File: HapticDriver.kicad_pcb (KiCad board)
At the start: 4 copper layers, 39 x 27 mm, 31 parts, among them J1 Conn_01x02_Socket, J14 USB_C_Receptacle_USB2.0, J3 BATT PWR, SW1 BOOT, SW2 EN, U1 ESP32-S3-WROOM-2, U12 DRV8912QPWPRQ1, U2 TPS561201DDCR, U3 DRV8912QPWPRQ1, U4 MAX98357A

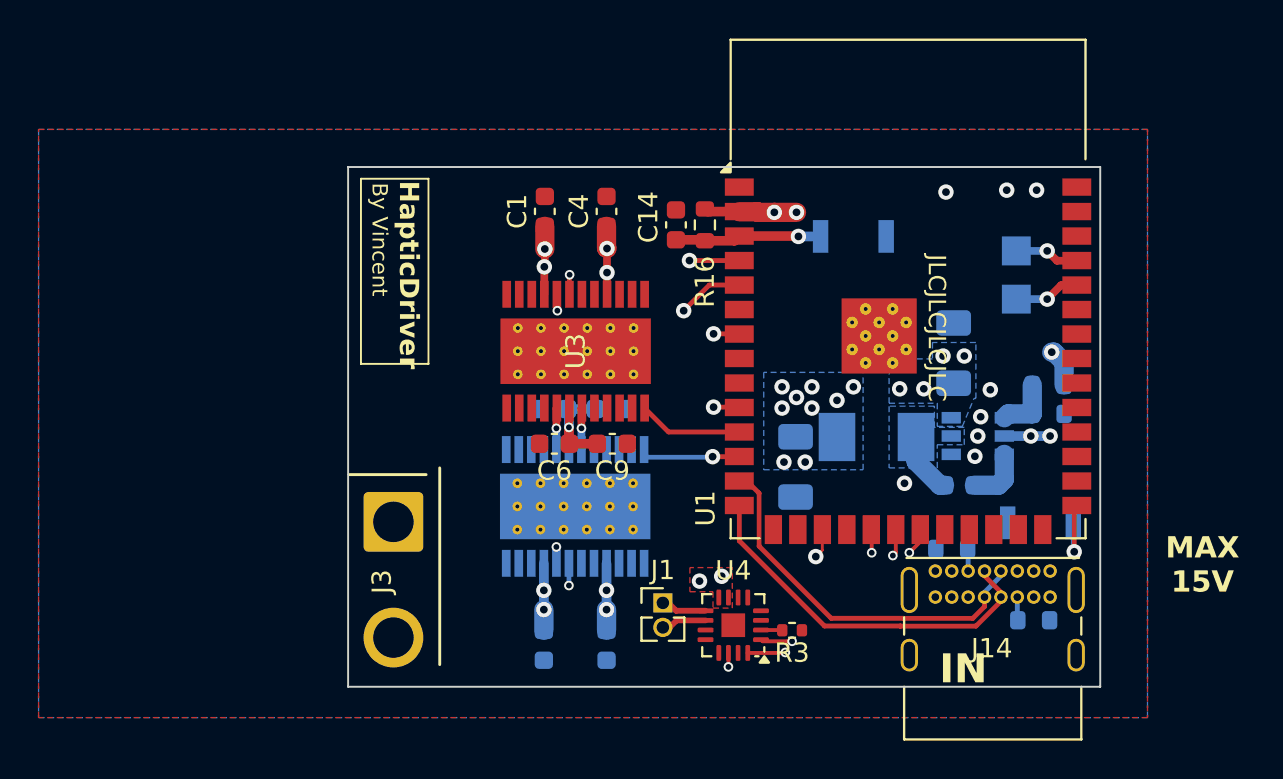
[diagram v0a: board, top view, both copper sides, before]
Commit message: feat: full reroute with max22200 driver
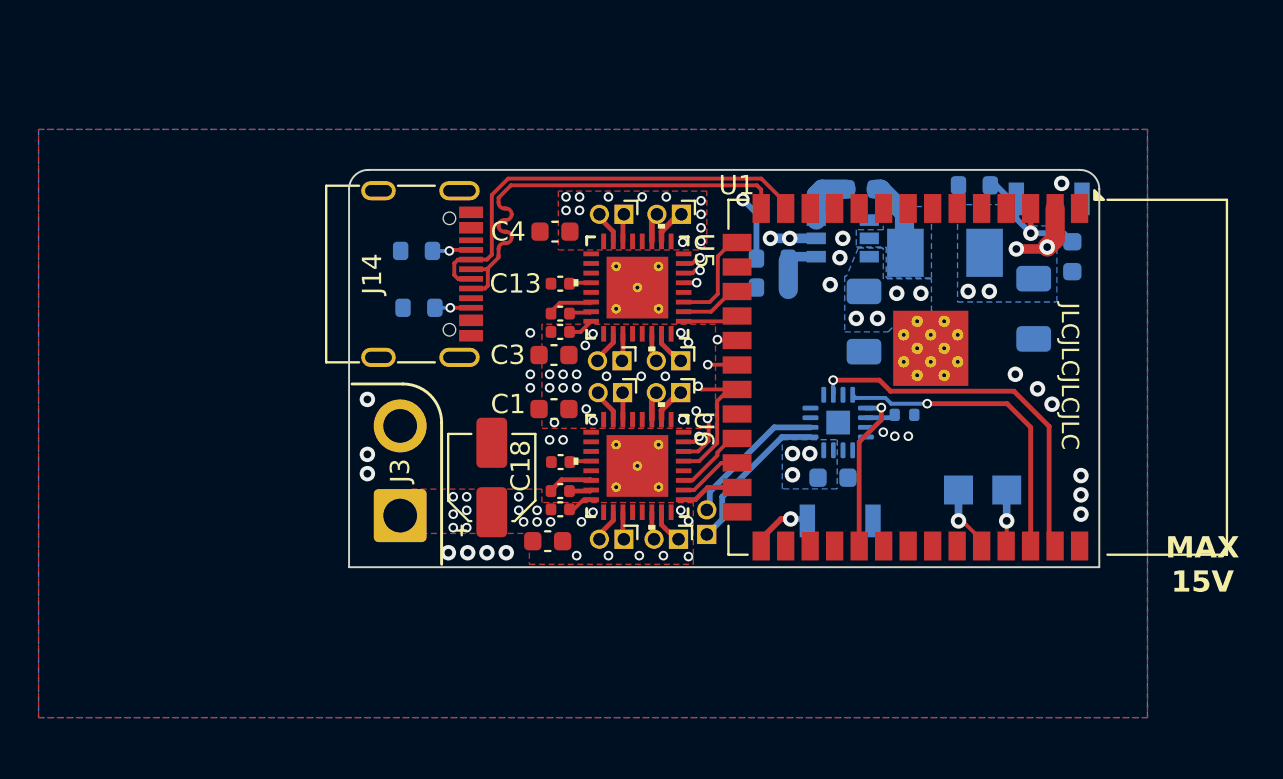
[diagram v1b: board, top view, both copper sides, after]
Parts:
- removed C22: 1uF, Capacitor_SMD:C_0603_1608Metric
- removed U12, U3: DRV8912QPWPRQ1, Ti:PWP0024N_N
- added C11: 0.1uF, Capacitor_SMD:C_0603_1608Metric, B.Cu at (148.2, 89.1)
- added C12: 0.1uF, Capacitor_SMD:C_0603_1608Metric, F.Cu at (133.4, 92.4)
- added C13: 22nF, Capacitor_SMD:C_0402_1005Metric, F.Cu at (134.1, 79.0)
- added C15: 22nF, Capacitor_SMD:C_0402_1005Metric, F.Cu at (134.1, 88.2)
- added C18: 10uF, Capacitor_SMD:CP_Elec_4x5.4, F.Cu at (130.5, 89.0)
- added J10: Conn_01x02_Pin, SolderWires:SolderWire_1x02, F.Cu at (137.3, 84.7)
- added J2: Conn_01x02_Pin, SolderWires:SolderWire_1x02, F.Cu at (140.3, 75.4)
- added J4: Conn_01x02_Pin, SolderWires:SolderWire_1x02, F.Cu at (140.3, 84.7)
- added J5: Conn_01x02_Pin, SolderWires:SolderWire_1x02, F.Cu at (140.3, 83.0)
- added J6: Conn_01x02_Pin, SolderWires:SolderWire_1x02, F.Cu at (140.2, 92.2)
- added J7: Conn_01x02_Pin, SolderWires:SolderWire_1x02, F.Cu at (137.2, 83.0)
- added J8: Conn_01x02_Pin, SolderWires:SolderWire_1x02, F.Cu at (137.3, 92.2)
- added J9: Conn_01x02_Pin, SolderWires:SolderWire_1x02, F.Cu at (137.3, 75.4)
- added U5: MAX22200ETJ+, AnalogDevices:21-0140AK_T3255_8C_MXM, F.Cu at (138.1, 79.2)
- added U6: MAX22200ETJ+, AnalogDevices:21-0140AK_T3255_8C_MXM, F.Cu at (138.1, 88.4)
- C14, R16, R3, U4: moved to B.Cu
- C2, C5: value 0.1uF -> 22nF; footprint Capacitor_SMD:C_0603_1608Metric -> Capacitor_SMD:C_0402_1005Metric; moved to F.Cu
- C3: moved to F.Cu
- C4: value 1uF -> 0.1uF
- C6, C9: value 0.1uF -> 1uF; footprint Capacitor_SMD:C_0603_1608Metric -> Capacitor_SMD:C_0402_1005Metric
- J1: footprint Connector_PinHeader_1.27mm:PinHeader_1x02_P1.27mm_Vertical -> SolderWires:SolderWire_1x02; moved to B.Cu
- J14: footprint Connector_USB:USB_C_Receptacle_GCT_USB4085 -> Connector_USB:USB_C_Receptacle_G-Switch_GT-USB-7010ASV
- J3: footprint Connector_Wire:SolderWire-1.5sqmm_1x02_P6mm_D1.7mm_OD3mm -> Connector_Wire:SolderWire-1sqmm_1x02_P5.4mm_D1.4mm_OD2.7mm
- moved R15 35.8 mm to (126.7, 80.2), turned to 0 degrees
- moved J14 31.8 mm to (125.7, 78.5), turned to -90 degrees
- moved R14 31.8 mm to (126.6, 77.3)
- moved C14 20.6 mm to (160.6, 77.6), turned to -90 degrees
- moved C10 16.2 mm to (149.7, 74.1), turned to 0 degrees
- moved R1 15.7 mm to (145.1, 77.7), turned to 0 degrees
- moved R2 15.7 mm to (145.1, 79.2), turned to 180 degrees
- moved C3 15.1 mm to (133.7, 82.7), turned to 180 degrees
- moved C8 14.8 mm to (158.6, 80.3)
- moved R16 14.1 mm to (155.5, 73.9), turned to 0 degrees
- moved R3 12.6 mm to (151.9, 85.8)
- moved U2 12.4 mm to (148.7, 76.7), turned to 180 degrees
- moved TP1 12.4 mm to (157.2, 89.7), turned to 0 degrees
- moved U4 11.8 mm to (148.5, 86.2)
- moved SW1 10.4 mm to (148.6, 91.3), turned to 0 degrees
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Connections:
- C2 pad 1: +3V3 -> Net-(U5B-CFN)
- C2 pad 2: GND -> Net-(U5B-CFP)
- C5 pad 1: +3V3 -> Net-(U6B-CFN)
- C5 pad 2: GND -> Net-(U6B-CFP)
- C6 pad 1: +3V3 -> +BATT
- C6 pad 2: GND -> Net-(U5B-VCP)
- C9 pad 1: +3V3 -> +BATT
- C9 pad 2: GND -> Net-(U6B-VCP)
- U1 pad 10: /DRV_MISO -> unconnected-(U1-GPIO17/U1TXD/ADC2_CH6-Pad10)
- U1 pad 11: /nFAULT_2 -> unconnected-(U1-GPIO18/U1RXD/ADC2_CH7/CLK_OUT3-Pad11)
- U1 pad 12: /nFAULT_1 -> unconnected-(U1-GPIO8/TOUCH8/ADC1_CH7/SUBSPICS1-Pad12)
- U1 pad 15: unconnected-(U1-GPIO3/TOUCH3/ADC1_CH2-Pad15) -> /DRV_CS_1
- U1 pad 17: /DRV_CS_1 -> /DRV_CMD_1
- U1 pad 18: unconnected-(U1-GPIO10/TOUCH10/ADC1_CH9/FSPICS0/FSPIIO4/SUBSPICS0-Pad18) -> /nFAULT_1
- U1 pad 19: /I2S_DIN -> /DRV_MISO
- U1 pad 20: /I2S_BCLK -> /DRV_MOSI
- U1 pad 21: /I2S_WCLK -> /DRV_SCK
- U1 pad 22: /DRV_SCL -> unconnected-(U1-GPIO14/TOUCH14/ADC2_CH3/FSPIWP/FSPIDQS/SUBSPIWP-Pad22)
- U1 pad 23: /DRV_SDA -> /DRV_CS_2
- U1 pad 24: unconnected-(U1-GPIO47/SPICLK_P/SUBSPICLK_P_DIFF-Pad24) -> /DRV_CMD_2
- U1 pad 25: unconnected-(U1-GPIO48/SPICLK_N/SUBSPICLK_N_DIFF-Pad25) -> /nFAULT_2
- U1 pad 31: unconnected-(U1-GPIO38/FSPIWP/SUBSPIWP-Pad31) -> /I2S_DIN
- U1 pad 38: unconnected-(U1-GPIO2/TOUCH2/ADC1_CH1-Pad38) -> /I2S_BCLK
- U1 pad 39: unconnected-(U1-GPIO1/TOUCH1/ADC1_CH0-Pad39) -> /I2S_WCLK
- U1 pad 4: /DRV_SCK -> unconnected-(U1-GPIO4/TOUCH4/ADC1_CH3-Pad4)
- U1 pad 5: /DRV_CS_2 -> unconnected-(U1-GPIO5/TOUCH5/ADC1_CH4-Pad5)
- U1 pad 7: /DRV_MOSI -> unconnected-(U1-GPIO7/TOUCH7/ADC1_CH6-Pad7)
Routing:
- net +3V3: track 13.8 -> 36.0 mm, vias 15 -> 8
- net +BATT: track 16.3 -> 3.12 mm, vias 14 -> 57
- net /DRV_SCK: track 26.1 -> 13.8 mm, vias 3 -> 2
- net /DRV_CS_1: track 16.8 -> 5.19 mm, vias 2 -> 0
- net /DRV_CS_2: track 12.0 -> 3.76 mm, vias 2 -> 0
- net Net-(J1-Pin_1): track 2.38 -> 8.23 mm
- net Net-(J1-Pin_2): track 2.36 -> 7.70 mm
- net /I2S_BCLK: track 11.0 -> 16.1 mm, vias 2 -> 1
- net /I2S_WCLK: track 14.0 -> 18.9 mm, vias 2 -> 1
- net /DRV_CMD_1: track 0.00 -> 3.53 mm
- net /USB_DP: track 19.7 -> 23.1 mm
- net /USB_DM: track 19.7 -> 23.2 mm
- net /DRV_CMD_2: track 0.00 -> 3.35 mm
- net /nFAULT_2: track 5.42 -> 3.04 mm
- net Net-(U6B-CFN): track 0.00 -> 2.37 mm
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- added copper zone on In2.Cu, net +3V3
- added copper zone on F.Cu, net +BATT
- added copper zone on In1.Cu, net GND
- removed copper zone on F.Cu, net +3V3
- removed copper zone on In1.Cu, net +3V3
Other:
- board size 39 x 27 mm -> 38.9 x 20.6 mm
- rule pad_to_mask_clearance: 0 -> 0.0001

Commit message: feat: fully routed v2 design
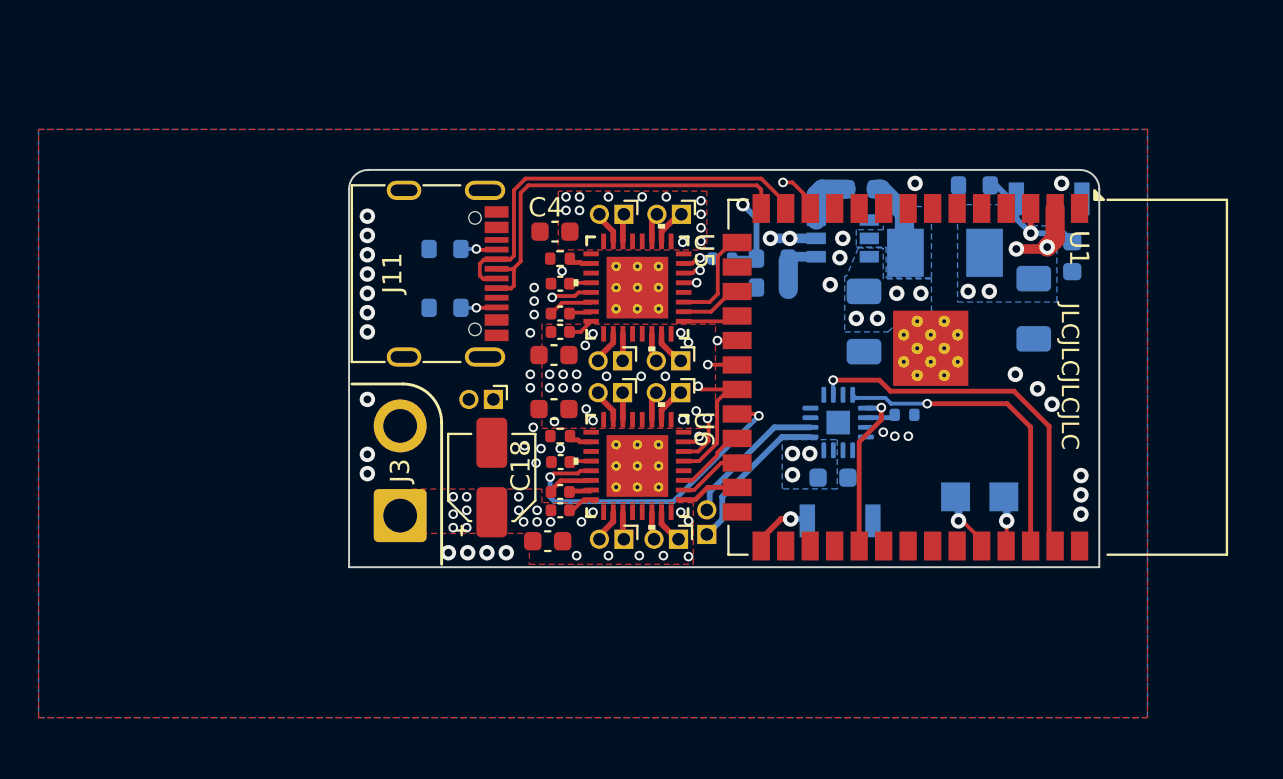
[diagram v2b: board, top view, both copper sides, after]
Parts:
- removed J14: USB_C_Receptacle_USB2.0, Connector_USB:USB_C_Receptacle_G-Switch_GT-USB-7010ASV
- added J11: USB_C_Receptacle_USB2.0_16P, Connector_USB:USB_C_Receptacle_G-Switch_GT-USB-7010ASV, F.Cu at (127.0, 78.5)
- added J12: Conn_01x02_Socket, SolderWires:SolderWire_1x02, F.Cu at (130.6, 85.0)
- added R4: 16K, Resistor_SMD:R_0402_1005Metric, F.Cu at (134.0, 77.7)
- added R5: 16K, Resistor_SMD:R_0402_1005Metric, F.Cu at (134.1, 86.9)
- added R6: 1K, Resistor_SMD:R_0402_1005Metric, B.Cu at (142.4, 77.7)
- moved R14 1.48 mm to (128.1, 77.2)
- moved R15 1.35 mm to (128.1, 80.2)
- moved TP1 0.38 mm to (157.1, 90.0)
- moved TP2 0.38 mm to (154.6, 90.0)
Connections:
- U1 pad 12: unconnected-(U1-GPIO8/TOUCH8/ADC1_CH7/SUBSPICS1-Pad12) -> /DRV_EN_1
- U1 pad 22: unconnected-(U1-GPIO14/TOUCH14/ADC2_CH3/FSPIWP/FSPIDQS/SUBSPIWP-Pad22) -> /DRV_EN_2
- U5 pad 18: unconnected-(U5A-IREF-Pad18) -> Net-(U5A-IREF)
- U5 pad 21: /Driver 1/nSLEEP -> /DRV_EN_1
- U6 pad 18: unconnected-(U6A-IREF-Pad18) -> Net-(U6A-IREF)
- U6 pad 21: /Driver 2/nSLEEP -> /DRV_EN_2
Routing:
- net /DRV_EN_1: track 0.00 -> 22.3 mm, vias 0 -> 2
- net /DRV_EN_2: track 0.00 -> 17.2 mm, vias 0 -> 2
- net /USB_DP: track 23.1 -> 20.5 mm
- net Net-(U5A-IREF): track 0.00 -> 1.16 mm
- net Net-(U6A-IREF): track 0.00 -> 1.13 mm
- net /USB_DM: track 23.2 -> 22.1 mm
- net +3V3: track 36.0 -> 36.9 mm
- net /DRV_MISO: track 13.2 -> 13.8 mm
- net GND: vias 25 -> 40
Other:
- board text added: "MAX 17V"
- board text removed: "MAX 15V"

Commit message: feat: battery level measurement resistors
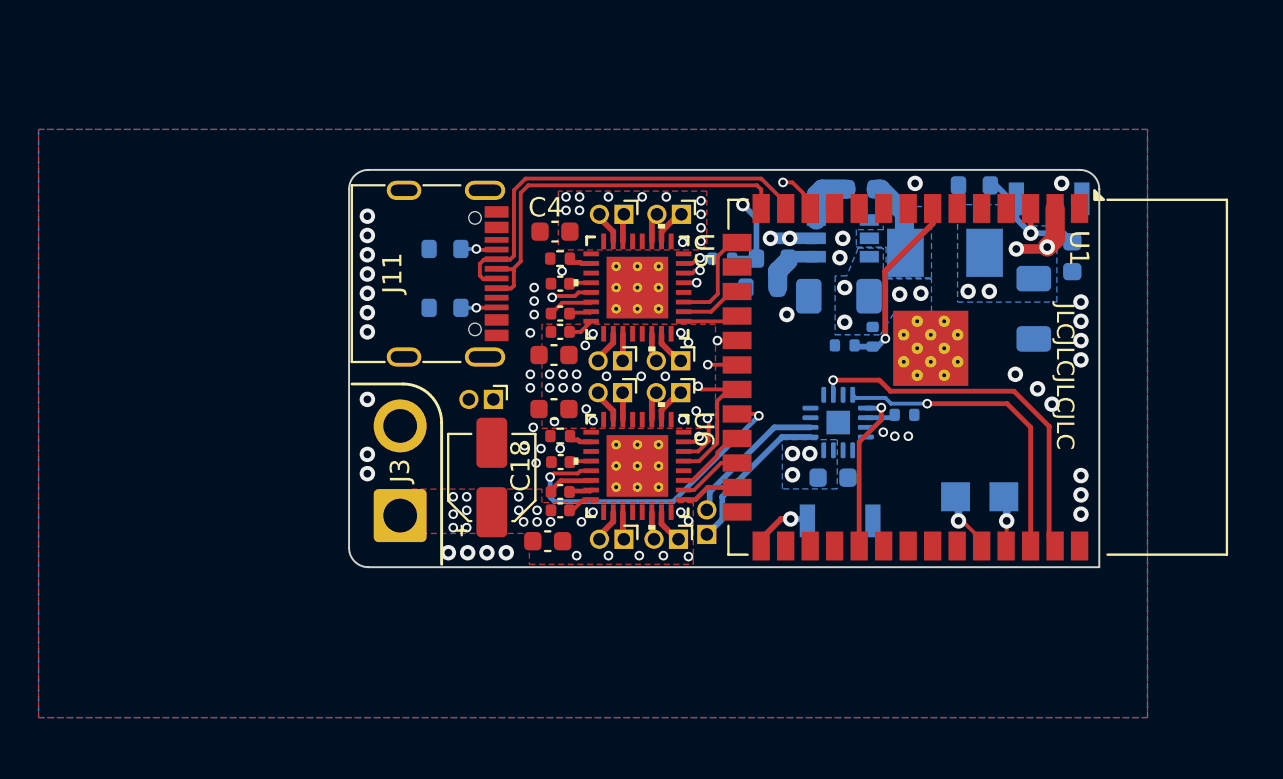
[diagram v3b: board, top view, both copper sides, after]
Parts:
- added R7: R_Small, Resistor_SMD:R_0402_1005Metric, B.Cu at (150.2, 81.8)
- added R8: R_Small, Resistor_SMD:R_0402_1005Metric, B.Cu at (148.8, 82.2)
- moved C7 1.85 mm to (148.5, 79.7), turned to 180 degrees
- moved R2 0.55 mm to (144.5, 79.2)
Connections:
- U1 pad 7: unconnected-(U1-GPIO7/TOUCH7/ADC1_CH6-Pad7) -> Net-(U1-GPIO7/TOUCH7/ADC1_CH6)
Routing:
- net Net-(U1-GPIO7/TOUCH7/ADC1_CH6): track 0.00 -> 9.57 mm, vias 0 -> 1
- net GND: vias 40 -> 44
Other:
- outline, holes or cut-outs redrawn

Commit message: feat: populate all jlcpcb part#
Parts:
- added R9: R, Resistor_SMD:R_0402_1005Metric, B.Cu at (148.8, 90.0)
- R7: value R_Small -> 16K
- R8: value R_Small -> 1K
- SW1, SW2: footprint Button_Omron:SW_B3U-1000P -> Button_Switch_SMD:SW_Push_1P1T_XKB_TS-1187A
- TP1: value TXD -> TX
- TP2: value RXD -> RX
- moved SW2 9.35 mm to (158.4, 83.9), turned to -90 degrees
- moved SW1 5.48 mm to (152.8, 87.8), turned to -90 degrees
- moved R3 2.82 mm to (149.6, 87.4), turned to 90 degrees
- moved TP1 2.40 mm to (159.4, 90.0)
- moved TP2 2.40 mm to (156.9, 90.0)
- moved C14 2.37 mm to (160.3, 75.2), turned to 0 degrees
- moved C8 2.27 mm to (159.4, 78.2), turned to 0 degrees
- moved U4 1.65 mm to (147.0, 86.9)
- moved C11 1.53 mm to (146.8, 89.8)
- moved R16 1.10 mm to (156.6, 73.9)
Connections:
- U1 pad 32: unconnected-(U1-MTCK/GPIO39/CLK_OUT3/SUBSPICS1-Pad32) -> /CODEC_MODE
- U4 pad 4: unconnected-(U4-~{SD_MODE}-Pad4) -> Net-(U4-~{SD_MODE})
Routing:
- net Net-(U1-GPIO0/BOOT): track 3.23 -> 13.9 mm
- net /EN: track 7.38 -> 16.2 mm
- net /CODEC_MODE: track 0.00 -> 3.63 mm, vias 0 -> 1
- net Net-(U4-~{SD_MODE}): track 0.00 -> 2.19 mm
- net Net-(U1-U0TXD/GPIO43/CLK_OUT1): track 2.91 -> 4.20 mm
- net /I2S_BCLK: track 16.1 -> 17.3 mm
- net /I2S_WCLK: track 18.9 -> 20.0 mm
- net Net-(J1-Pin_2): track 7.70 -> 6.63 mm
- net Net-(J1-Pin_1): track 8.23 -> 7.29 mm
- net Net-(U1-U0RXD/GPIO44/CLK_OUT2): track 3.51 -> 2.87 mm
- net GND: vias 44 -> 45
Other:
- board text added: "MAX 16V"
- board text removed: "MAX 17V"
